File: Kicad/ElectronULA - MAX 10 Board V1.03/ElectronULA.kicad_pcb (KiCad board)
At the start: 4 copper layers, 49 x 68.4 mm, 72 parts, among them J1 Conn_01x02, SW1 SW_DIP_x04, U1 10M08SCE144C8G, U10 SN74HCT125D, U2 74LVC4245APW, U3 74LVC4245APW, U4 74LVC4245APW, U5 74LVC4245APW, U6 74LVC4245APW, U7 74LVC4245APW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

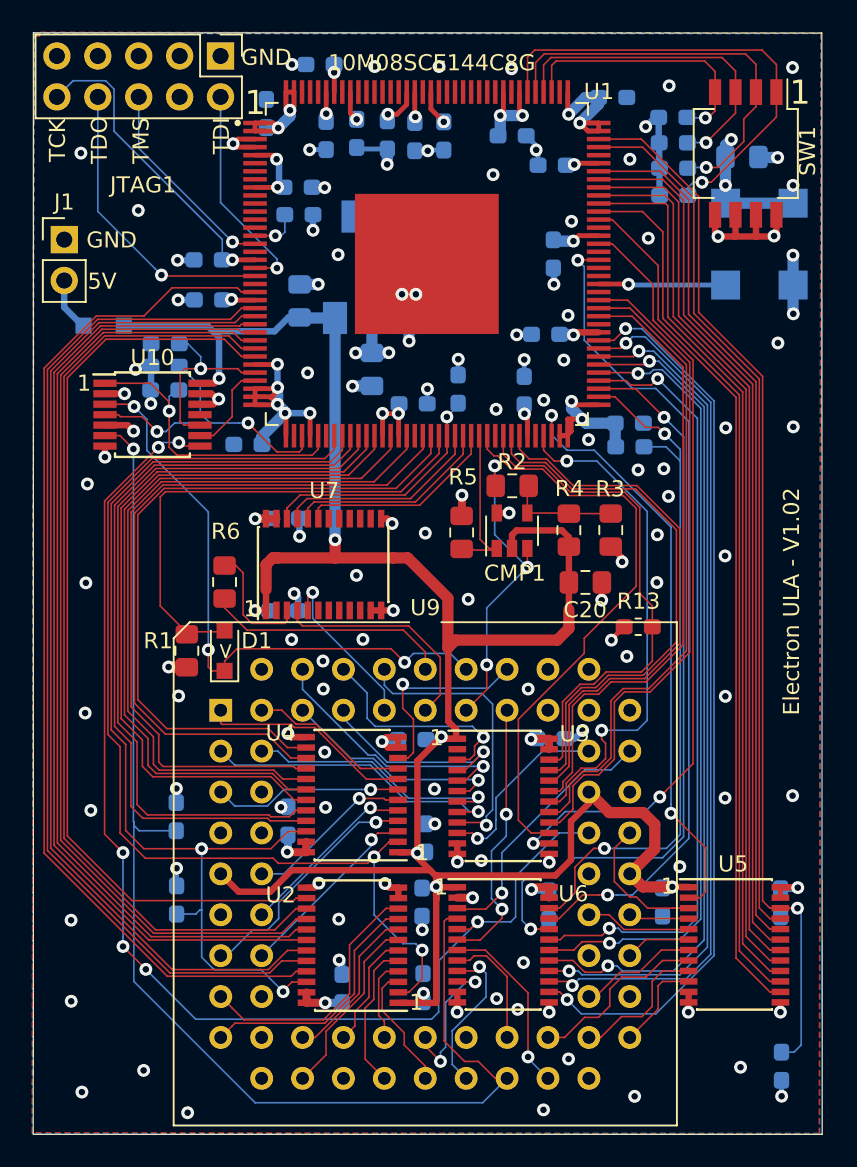
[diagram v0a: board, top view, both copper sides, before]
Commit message: Added 4.7K pullups for the keyboard Inputs
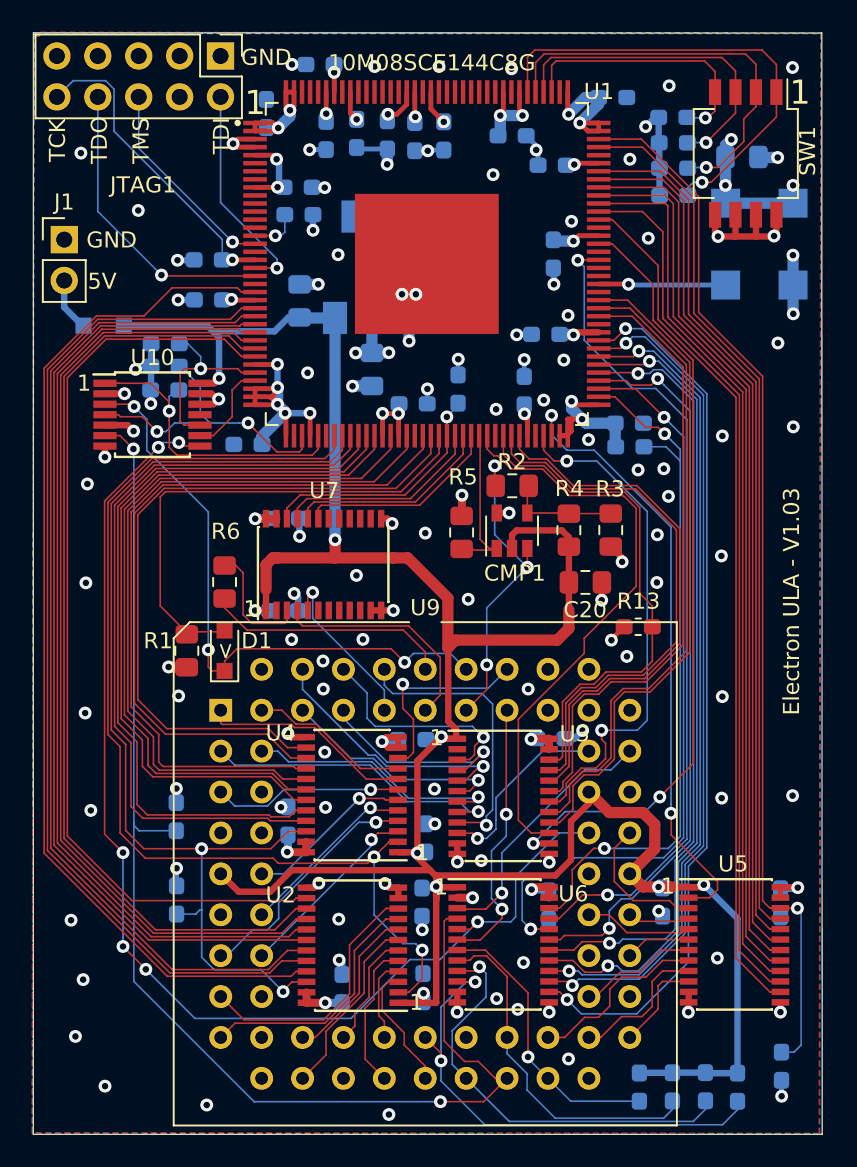
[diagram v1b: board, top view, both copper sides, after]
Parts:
- added R26: 4.7K, Resistor_SMD:R_0603_1608Metric_Pad1.05x0.95mm_HandSolder, B.Cu at (167.3, 121.7)
- added R27: 4.7K, Resistor_SMD:R_0603_1608Metric_Pad1.05x0.95mm_HandSolder, B.Cu at (169.4, 121.7)
- added R28: 4.7K, Resistor_SMD:R_0603_1608Metric_Pad1.05x0.95mm_HandSolder, B.Cu at (171.4, 121.7)
- added R29: 4.7K, Resistor_SMD:R_0603_1608Metric_Pad1.05x0.95mm_HandSolder, B.Cu at (173.4, 121.7)
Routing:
- net /KBD0: track 9.23 -> 30.9 mm
- net /5V: track 146.5 -> 165.9 mm, vias 8 -> 9
- net /KBD1: track 9.88 -> 26.7 mm
- net /KBD2: track 7.59 -> 21.9 mm
- net /KBD3: track 11.4 -> 17.6 mm
- net /LVRnWIN: track 48.4 -> 45.4 mm
- net /LVKBD1: track 54.2 -> 52.1 mm
- net /RnW: track 76.1 -> 74.2 mm
- net /LVKBD2: track 52.6 -> 50.7 mm
- net /LVKBD3: track 51.9 -> 50.3 mm
- net /LVKBD0: track 56.1 -> 55.0 mm
- net /PD_DIR: track 37.0 -> 38.0 mm
- net /LVnNMI: track 49.5 -> 48.5 mm
- net /nIRQ: track 78.3 -> 78.2 mm, vias 1 -> 2
- net /GND: vias 109 -> 108
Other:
- board text added: "Electron ULA - V1.03"
- board text removed: "Electron ULA - V1.02"
